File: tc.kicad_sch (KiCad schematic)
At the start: 7 parts

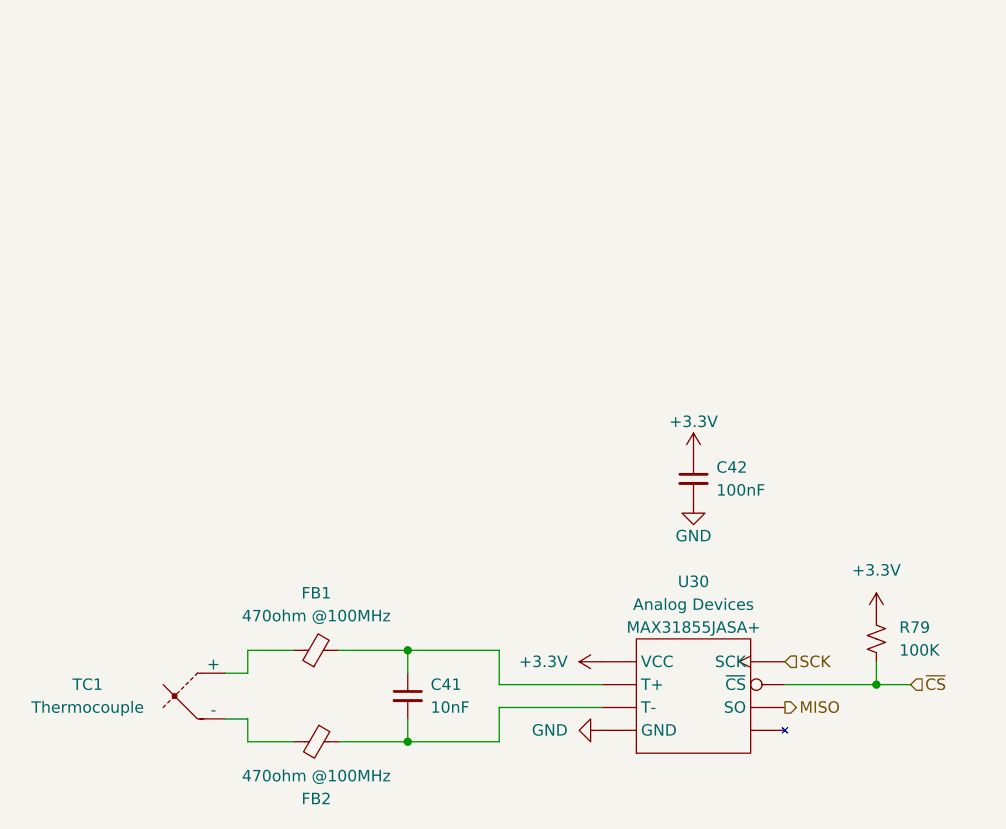
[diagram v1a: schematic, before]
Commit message: Deleted 5V, edited LPFs on TCs and PTs
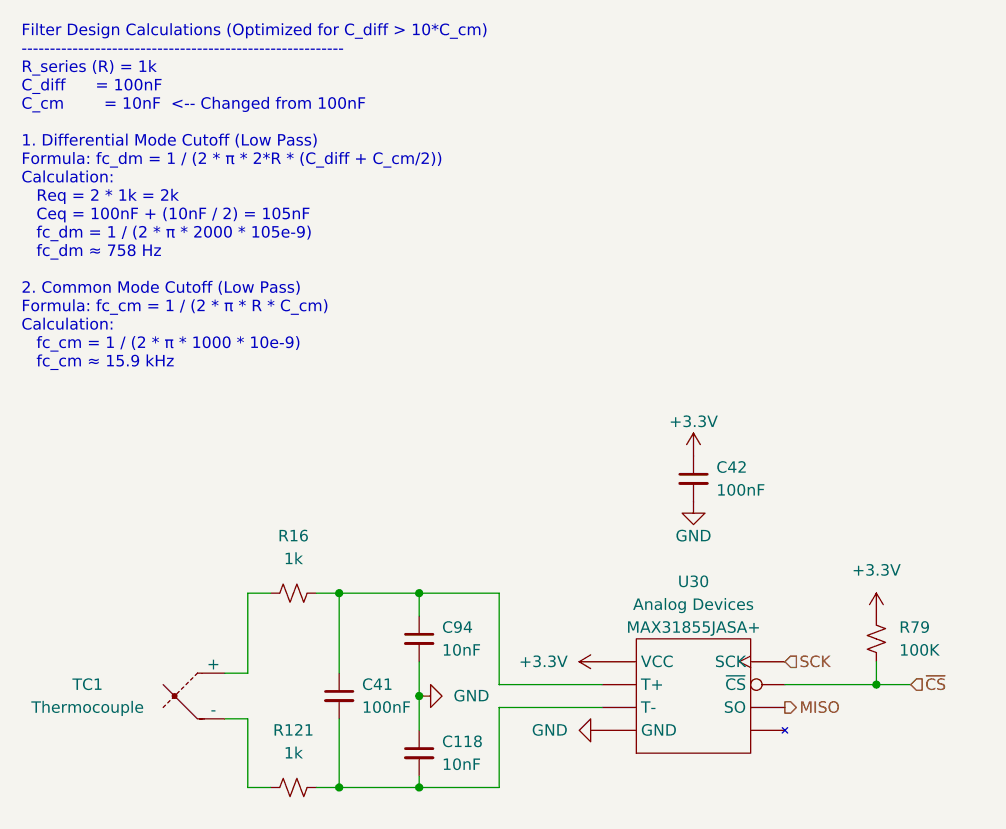
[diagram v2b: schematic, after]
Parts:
- removed FB1, FB2: 470ohm @100MHz, Inductor_SMD:L_0603_1608Metric, symbol Device:FerriteBead_Small
- added C118, C94: 10nF, Capacitor_SMD:C_0402_1005Metric, symbol Device:C_Small
- added R121, R16: 1k, Resistor_SMD:R_0402_1005Metric, symbol Device:R_Small_US
- C41: value 10nF -> 100nF
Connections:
- net GND: now also C118.1, C94.2
- net at TC1.1 (+): now also R16.1
- net at C41.1, U30.3 (T+): now also C94.1, R16.2
- net at C41.2, U30.2 (T-): now also C118.2, R121.2
- net at TC1.2 (-): now also R121.1
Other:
- note added: "Filter Design Calculations (Optimized for C_diff > 10*C_cm) --------------------------------------------------------- R_series (R) = 1k C_diff = 100nF C_cm = 10nF <-- Changed from 100nF 1. Differential Mode Cutoff (Low Pass) Formula: fc_dm = 1 / (2 * π * 2*R * (C_diff + C_cm/2)) Calculation: Req = 2 * 1k = 2k Ceq = 100nF + (10nF / 2) = 105nF fc_dm = 1 / (2 * π * 2000 * 105e-9) fc_dm ≈ 758 Hz 2. C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"
- moved on the sheet: C41

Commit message: version in PCBway 12/12/2025
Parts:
- C41: Part # Generic CAP CER 10NF 6.3V X7R 0402 -> Generic CAP CER 0.1UF 6.3V X7R 0402
- R121, R16: Part # (none) -> Generic RES SMD 1K OHM 1% 1/16W 0402
- TC1: now not fitted
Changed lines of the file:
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@@
 		(in_bom yes)
 		(on_board yes)
-		(dnp no)
+		(dnp yes)
 		(property "Reference" "TC1"
 			(at 85.09 100.33 0)
@@
 			)
 		)
+		(property "Part #" "Generic RES SMD 1K OHM 1% 1/16W 0402"
+			(at 107.95 111.76 90)
+			(effects
+				(font
+					(size 1.27 1.27)
+				)
+				(hide yes)
+			)
+		)
 		(pin "2"
 		)
@@
 			)
 		)
-		(property "Part #" "Generic CAP CER 10NF 6.3V X7R 0402"
+		(property "Part #" "Generic CAP CER 0.1UF 6.3V X7R 0402"
 			(at 113.03 101.6 0)
 			(effects
@@
 			(effects
 				(font
+					(size 1.27 1.27)
+				)
+				(hide yes)
+			)
+		)
+		(property "Part #" "Generic RES SMD 1K OHM 1% 1/16W 0402"
+			(at 107.95 90.17 90)
+			(effects
+				(font

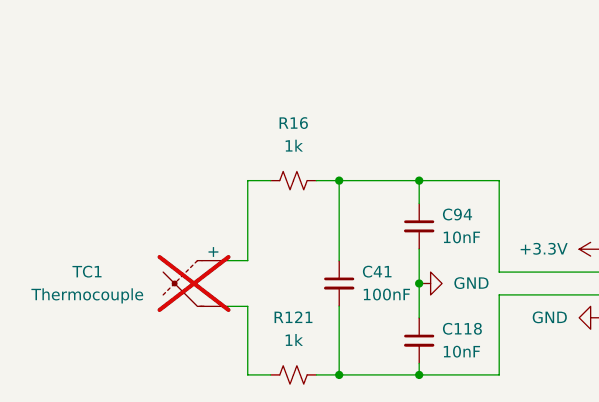
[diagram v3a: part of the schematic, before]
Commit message: changed charging circuit for Insta360, gonna send in now on JLCPCB
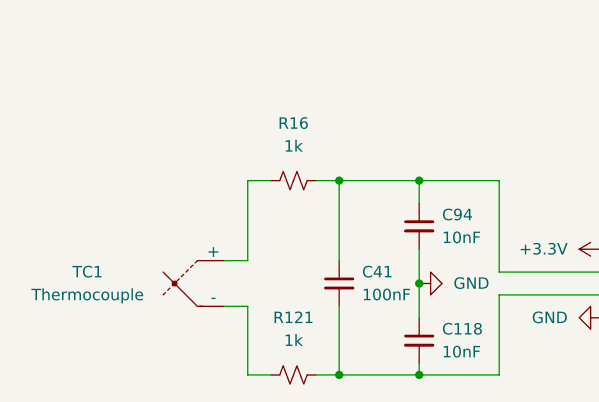
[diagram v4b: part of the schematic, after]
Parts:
- TC1: now fitted
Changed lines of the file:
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@@
 			)
 		)
-		(property "Description" ""
+		(property "Description" "Power symbol creates a global label with name \"GND\" , ground"
 			(at 121.92 101.6 0)
 			(effects
@@
 			)
 		)
-		(property "Description" ""
+		(property "Description" "Power symbol creates a global label with name \"+3.3V\""
 			(at 152.4 74.93 0)
 			(effects
@@
 			)
 		)
-		(property "Description" ""
+		(property "Description" "Power symbol creates a global label with name \"GND\" , ground"
 			(at 142.24 105.41 0)
 			(effects
@@
 			)
 		)
-		(property "Description" ""
+		(property "Description" "Unpolarized capacitor, small symbol"
 			(at 121.92 95.25 0)
 			(effects
@@
 		(in_bom yes)
 		(on_board yes)
-		(dnp yes)
+		(dnp no)
 		(property "Reference" "TC1"
 			(at 85.09 100.33 0)
@@
 			)
 		)
-		(property "Datasheet" "https://www.farnell.com/datasheets/4071246.pdf"
+		(property "Datasheet" "~"
 			(at 83.185 100.33 0)
 			(effects
@@
 			)
 		)
-		(property "Description" ""
+		(property "Description" "Thermocouple"
 			(at 97.79 101.6 0)
 			(effects
@@
 			)
 		)
-		(property "Description" ""
+		(property "Description" "Unpolarized capacitor, small symbol"
 			(at 152.4 77.47 0)
 			(effects
@@
 			)
 		)
-		(property "Description" ""
+		(property "Description" "Power symbol creates a global label with name \"+3.3V\""
 			(at 142.24 97.79 0)
 			(effects
@@
 			)
 		)
-		(property "Description" ""
+		(property "Description" "Resistor, small US symbol"
 			(at 172.72 95.25 0)
 			(effects
@@
 			)
 		)
-		(property "Description" ""
+		(property "Description" "Unpolarized capacitor, small symbol"
 			(at 121.92 107.95 0)
 			(effects
@@
 			)
 		)
-		(property "Description" ""
+		(property "Description" "Unpolarized capacitor, small symbol"
 			(at 113.03 101.6 0)
 			(effects
@@
 			)
 		)
-		(property "Description" ""
+		(property "Description" "Power symbol creates a global label with name \"GND\" , ground"
 			(at 152.4 80.01 0)
 			(effects
